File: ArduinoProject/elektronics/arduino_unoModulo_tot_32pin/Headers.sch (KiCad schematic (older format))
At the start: 4 parts, among them J201 POWER, J202 IOL, J203 AD, J204 IOL

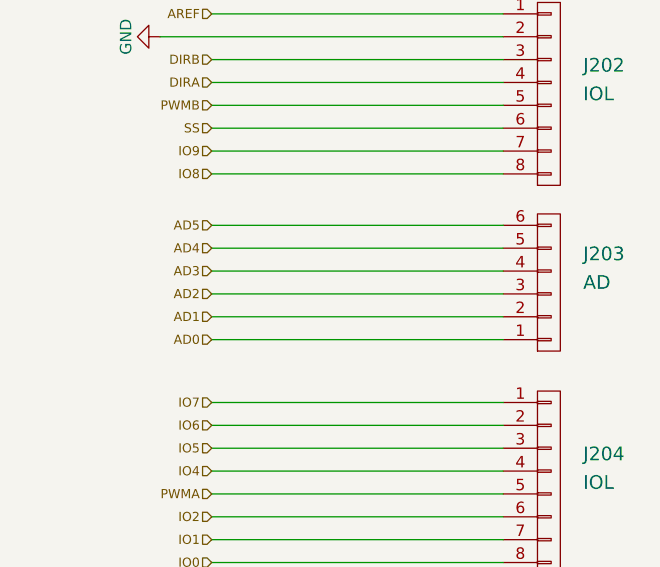
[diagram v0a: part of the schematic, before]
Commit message: analog pins added
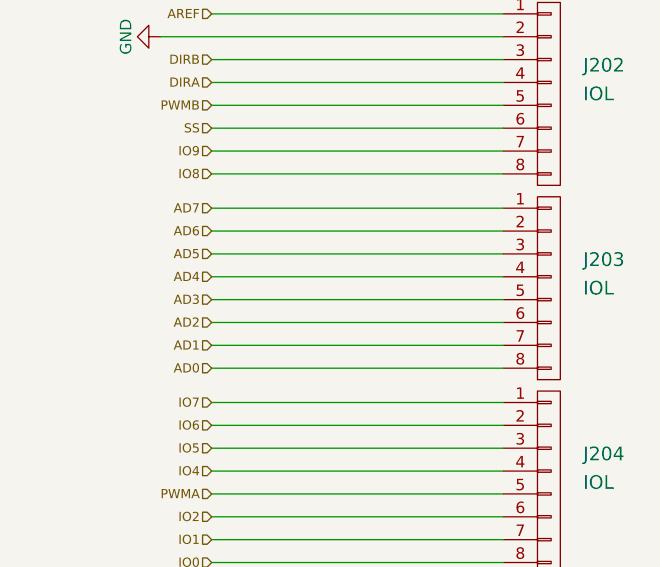
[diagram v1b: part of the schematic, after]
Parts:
- removed J203: AD, Socket_Strips:Socket_Strip_Straight_1x08_Pitch2.00mm, symbol CONN_01X06
- added J203: IOL, Socket_Strips:Socket_Strip_Angled_1x08_Pitch2.00mm, symbol CONN_01X08
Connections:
- net AD0: now also J203.8 (P8)
- net AD1: now also J203.7 (P7)
- net AD2: now also J203.6 (P6)
- net AD3: now also J203.5 (P5)
- net AD4: now also J203.4 (P4)
- net AD5: now also J203.3 (P3)
- new net AD6: J203.2 (P2)
- new net AD7: J203.1 (P1)
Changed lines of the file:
@@
 Comment4 ""
 $EndDescr
-$Comp
-L CONN_01X06 J203
-U 1 1 55E94764
-P 6250 4650
-F 0 "J203" H 6400 4525 60  0000 L CNN
-F 1 "AD" H 6400 4650 60  0000 L CNN
-F 2 "Socket_Strips:Socket_Strip_Straight_1x08_Pitch2.00mm" H 6250 4650 60  0001 C CNN
-F 3 "http://sullinscorp.com/catalogs/101_PAGE114-115_.100_FEMALE_HDR.pdf" H 6250 4650 60  0001 C CNN
-F 4 "Connector Header 6 Position 0.100\" (2.54mm) Gold Surface Mount" H 6250 4650 60  0001 C CNN "Characteristics"
-F 5 "Shield Header 6POS - ANLG" H 6250 4650 60  0001 C CNN "Description"
-F 6 "Sullins Connector" H 6250 4650 60  0001 C CNN "MFN"
-F 7 "NPPC061KFXC-RC" H 6250 4650 60  0001 C CNN "MFP"
-F 8 "SMD" H 6250 4650 60  0001 C CNN "Package ID"
-F 9 "ANY" H 6250 4650 60  0001 C CNN "Source"
-F 10 "N" H 6250 4650 60  0001 C CNN "Critical"
-F 11 "Shield_Headers" H 6250 4650 60  0001 C CNN "Subsystem"
-F 12 "~" H 6250 4650 60  0001 C CNN "Notes"
-	1    6250 4650
-	1    0    0    1
-$EndComp
-Text HLabel 4775 4600 0    40   Input ~ 0
+Text HLabel 4775 4725 0    40   Input ~ 0
 AD3
-Text HLabel 4775 4700 0    40   Input ~ 0
+Text HLabel 4775 4825 0    40   Input ~ 0
 AD2
-Text HLabel 4775 4800 0    40   Input ~ 0
+Text HLabel 4775 4925 0    40   Input ~ 0
 AD1
-Text HLabel 4775 4900 0    40   Input ~ 0
+Text HLabel 4775 5025 0    40   Input ~ 0
 AD0
 Text HLabel 4775 5175 0    40   Input ~ 0
@@
 $EndComp
 Wire Wire Line
-	4775 4900 6050 4900
-Wire Wire Line
-	6050 4800 4775 4800
-Wire Wire Line
-	4775 4700 6050 4700
-Wire Wire Line
-	6050 4600 4775 4600
+	4775 5025 6050 5025
+Wire Wire Line
+	6050 4925 4775 4925
+Wire Wire Line
+	4775 4825 6050 4825
+Wire Wire Line
+	6050 4725 4775 4725
 Wire Wire Line
 	6050 5175 4775 5175
@@
 Wire Wire Line
 	4775 5875 6050 5875
-Text HLabel 4775 4400 0    40   Input ~ 0
+Text HLabel 4775 4525 0    40   Input ~ 0
 AD5
-Text HLabel 4775 4500 0    40   Input ~ 0
+Text HLabel 4775 4625 0    40   Input ~ 0
 AD4
 Wire Wire Line
-	6050 4400 4775 4400
-Wire Wire Line
-	6050 4500 4775 4500
+	6050 4525 4775 4525
+Wire Wire Line
+	6050 4625 4775 4625
 Text HLabel 4775 3475 0    40   Input ~ 0
 AREF
@@
 	1    0    0    -1
 $EndComp
+$Comp
+L CONN_01X08 J203
+U 1 1 5A9EE64C
+P 6250 4675
+F 0 "J203" H 6400 4800 60  0000 L CNN
+F 1 "IOL" H 6400 4675 60  0000 L CNN
+F 2 "Socket_Strips:Socket_Strip_Angled_1x08_Pitch2.00mm" H 6250 4675 60  0001 C CNN
+F 3 "http://sullinscorp.com/catalogs/101_PAGE114-115_.100_FEMALE_HDR.pdf" H 6250 4675 60  0001 C CNN
+F 4 "Connector Header 8 Position 0.100\" (2.54mm) Gold Surface Mount" H 6250 4675 60  0001 C CNN "Characteristics"
+F 5 "Shield Header 8POS - DIG01" H 6250 4675 60  0001 C CNN "Description"
+F 6 "Sullins Connector" H 6250 4675 60  0001 C CNN "MFN"
+F 7 "NPPC081KFXC-RC" H 6250 4675 60  0001 C CNN "MFP"
+F 8 "SMD" H 6250 4675 60  0001 C CNN "Package ID"
+F 9 "ANY" H 6250 4675 60  0001 C CNN "Source"
+F 10 "N" H 6250 4675 60  0001 C CNN "Critical"
+F 11 "Shield_Headers" H 6250 4675 60  0001 C CNN "Subsystem"
+F 12 "~" H 6250 4675 60  0001 C CNN "Notes"
+	1    6250 4675
+	1    0    0    -1
+$EndComp
+Text HLabel 4775 4325 0    40   Input ~ 0
+AD7
+Text HLabel 4775 4425 0    40   Input ~ 0
+AD6
+Wire Wire Line
+	6050 4325 4775 4325
+Wire Wire Line
+	6050 4425 4775 4425
 $EndSCHEMATC

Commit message: sensormodule_x4 added
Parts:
- J201: footprint Socket_Strips:Socket_Strip_Angled_1x06_Pitch2.00mm -> Socket_Strips:Socket_Strip_Straight_1x06_Pitch2.00mm
- J202, J203, J204: footprint Socket_Strips:Socket_Strip_Angled_1x08_Pitch2.00mm -> Socket_Strips:Socket_Strip_Straight_1x08_Pitch2.00mm
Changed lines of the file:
@@
 LIBS:MFN_Atmel
 LIBS:MFN_STMicro
+LIBS:degson
 LIBS:Arduino_Uno_R3_From_Scratch-cache
 EELAYER 25 0
@@
 F 0 "J204" H 6400 5650 60  0000 L CNN
 F 1 "IOL" H 6400 5525 60  0000 L CNN
-F 2 "Socket_Strips:Socket_Strip_Angled_1x08_Pitch2.00mm" H 6250 5525 60  0001 C CNN
+F 2 "Socket_Strips:Socket_Strip_Straight_1x08_Pitch2.00mm" H 6250 5525 60  0001 C CNN
 F 3 "http://sullinscorp.com/catalogs/101_PAGE114-115_.100_FEMALE_HDR.pdf" H 6250 5525 60  0001 C CNN
 F 4 "Connector Header 8 Position 0.100\" (2.54mm) Gold Surface Mount" H 6250 5525 60  0001 C CNN "Characteristics"
@@
 F 0 "J202" H 6400 3950 60  0000 L CNN
 F 1 "IOL" H 6400 3825 60  0000 L CNN
-F 2 "Socket_Strips:Socket_Strip_Angled_1x08_Pitch2.00mm" H 6250 3825 60  0001 C CNN
+F 2 "Socket_Strips:Socket_Strip_Straight_1x08_Pitch2.00mm" H 6250 3825 60  0001 C CNN
 F 3 "http://sullinscorp.com/catalogs/101_PAGE114-115_.100_FEMALE_HDR.pdf" H 6250 3825 60  0001 C CNN
 F 4 "Connector Header 8 Position 0.100\" (2.54mm) Gold Surface Mount" H 6250 3825 60  0001 C CNN "Characteristics"
@@
 F 0 "J201" H 2550 1850 60  0000 L CNN
 F 1 "POWER" H 2550 1975 60  0000 L CNN
-F 2 "Socket_Strips:Socket_Strip_Angled_1x06_Pitch2.00mm" H 2400 1975 60  0001 C CNN
+F 2 "Socket_Strips:Socket_Strip_Straight_1x06_Pitch2.00mm" H 2400 1975 60  0001 C CNN
 F 3 "http://sullinscorp.com/catalogs/101_PAGE114-115_.100_FEMALE_HDR.pdf" H 2400 1975 60  0001 C CNN
 F 4 "Connector Header 6 Position 0.100\" (2.54mm) Gold Surface Mount" H 2400 1975 60  0001 C CNN "Characteristics"
@@
 F 0 "J203" H 6400 4800 60  0000 L CNN
 F 1 "IOL" H 6400 4675 60  0000 L CNN
-F 2 "Socket_Strips:Socket_Strip_Angled_1x08_Pitch2.00mm" H 6250 4675 60  0001 C CNN
+F 2 "Socket_Strips:Socket_Strip_Straight_1x08_Pitch2.00mm" H 6250 4675 60  0001 C CNN
 F 3 "http://sullinscorp.com/catalogs/101_PAGE114-115_.100_FEMALE_HDR.pdf" H 6250 4675 60  0001 C CNN
 F 4 "Connector Header 8 Position 0.100\" (2.54mm) Gold Surface Mount" H 6250 4675 60  0001 C CNN "Characteristics"

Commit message: new components
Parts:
- J201: footprint Socket_Strips:Socket_Strip_Straight_1x06_Pitch2.00mm -> Socket_Strips:Socket_Strip_Straight_1x06_Pitch2.54mm
- J202, J203, J204: footprint Socket_Strips:Socket_Strip_Straight_1x08_Pitch2.00mm -> Socket_Strips:Socket_Strip_Straight_1x08_Pitch2.54mm
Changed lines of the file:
@@
 F 0 "J204" H 6400 5650 60  0000 L CNN
 F 1 "IOL" H 6400 5525 60  0000 L CNN
-F 2 "Socket_Strips:Socket_Strip_Straight_1x08_Pitch2.00mm" H 6250 5525 60  0001 C CNN
+F 2 "Socket_Strips:Socket_Strip_Straight_1x08_Pitch2.54mm" H 6250 5525 60  0001 C CNN
 F 3 "http://sullinscorp.com/catalogs/101_PAGE114-115_.100_FEMALE_HDR.pdf" H 6250 5525 60  0001 C CNN
 F 4 "Connector Header 8 Position 0.100\" (2.54mm) Gold Surface Mount" H 6250 5525 60  0001 C CNN "Characteristics"
@@
 F 0 "J202" H 6400 3950 60  0000 L CNN
 F 1 "IOL" H 6400 3825 60  0000 L CNN
-F 2 "Socket_Strips:Socket_Strip_Straight_1x08_Pitch2.00mm" H 6250 3825 60  0001 C CNN
+F 2 "Socket_Strips:Socket_Strip_Straight_1x08_Pitch2.54mm" H 6250 3825 60  0001 C CNN
 F 3 "http://sullinscorp.com/catalogs/101_PAGE114-115_.100_FEMALE_HDR.pdf" H 6250 3825 60  0001 C CNN
 F 4 "Connector Header 8 Position 0.100\" (2.54mm) Gold Surface Mount" H 6250 3825 60  0001 C CNN "Characteristics"
@@
 F 0 "J201" H 2550 1850 60  0000 L CNN
 F 1 "POWER" H 2550 1975 60  0000 L CNN
-F 2 "Socket_Strips:Socket_Strip_Straight_1x06_Pitch2.00mm" H 2400 1975 60  0001 C CNN
+F 2 "Socket_Strips:Socket_Strip_Straight_1x06_Pitch2.54mm" H 2400 1975 60  0001 C CNN
 F 3 "http://sullinscorp.com/catalogs/101_PAGE114-115_.100_FEMALE_HDR.pdf" H 2400 1975 60  0001 C CNN
 F 4 "Connector Header 6 Position 0.100\" (2.54mm) Gold Surface Mount" H 2400 1975 60  0001 C CNN "Characteristics"
@@
 F 0 "J203" H 6400 4800 60  0000 L CNN
 F 1 "IOL" H 6400 4675 60  0000 L CNN
-F 2 "Socket_Strips:Socket_Strip_Straight_1x08_Pitch2.00mm" H 6250 4675 60  0001 C CNN
+F 2 "Socket_Strips:Socket_Strip_Straight_1x08_Pitch2.54mm" H 6250 4675 60  0001 C CNN
 F 3 "http://sullinscorp.com/catalogs/101_PAGE114-115_.100_FEMALE_HDR.pdf" H 6250 4675 60  0001 C CNN
 F 4 "Connector Header 8 Position 0.100\" (2.54mm) Gold Surface Mount" H 6250 4675 60  0001 C CNN "Characteristics"
